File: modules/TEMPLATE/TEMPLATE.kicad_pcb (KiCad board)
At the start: 2 copper layers, 160 x 100 mm, 2 parts, among them J1 Card_Connector

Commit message: adsr additions
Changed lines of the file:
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@@
 		(rev "A")
 		(company "THE HOUSE OF GALAHAD")
-		(comment 1 "FORMANT-KO")
+		(comment 1 "FORMANT^{KO}")
 	)
 	(layers

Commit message: vc-lfo schematic; pcb start
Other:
- board text added: "${COMMENT1} ${TITLE}"
- board text added: "| ${COMMENT2} | ${COMMENT3} | ${COMMENT4} |"
- board text added: "| ${COMPANY} | ${COMMENT1} ${TITLE} | REV ${REVISION} | ${ISSUE_DATE} |"
- board text added: "| ${TITLE} | ${COMMENT5} |"
- board text removed: "| ${COMPANY} | ${COMMENT1} ${TITLE} | REVISION ${REVISION} | ${ISSUE_DATE} |"
- board text removed: "| ${EMAIL} | ${GITHUB} | ${TAG} |"
- board text removed: "| ${MODULE} | ${PARTNO} |"

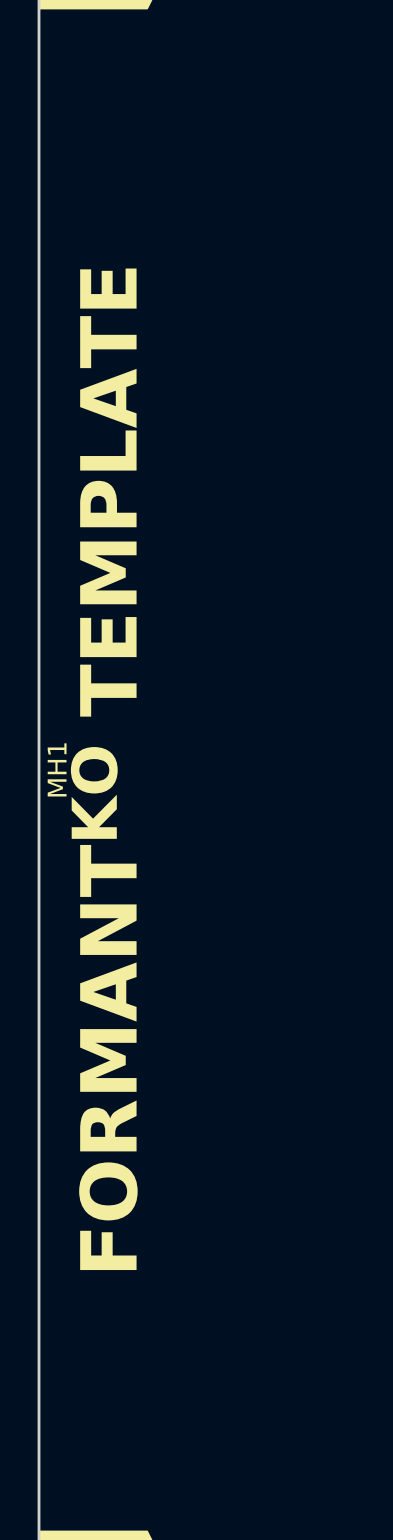
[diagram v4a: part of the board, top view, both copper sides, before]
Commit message: com updates for new templates and styles
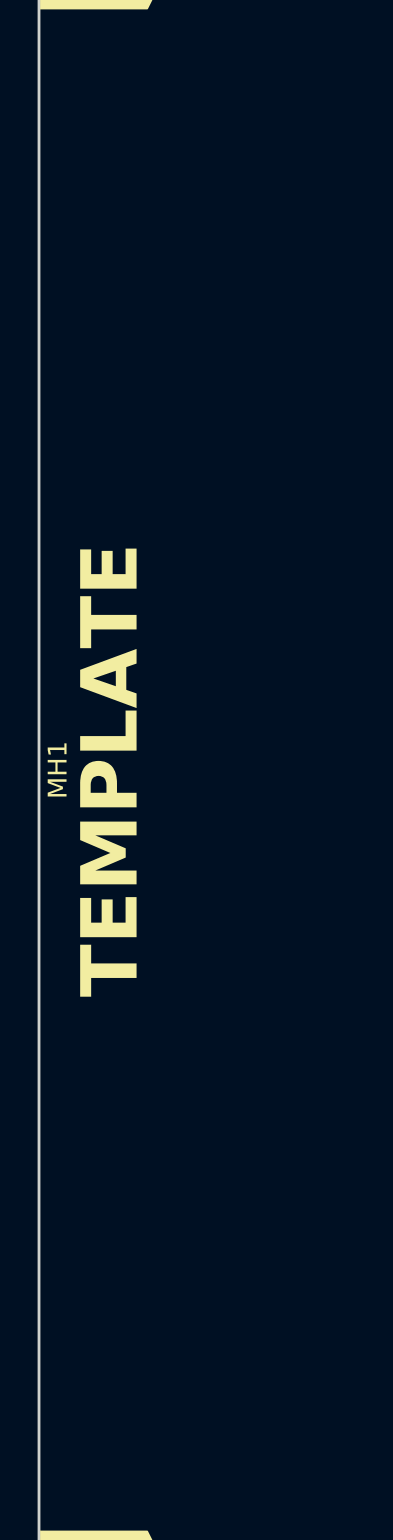
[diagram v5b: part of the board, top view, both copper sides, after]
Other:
- board text added: "${TITLE}"
- board text removed: "${COMMENT1} ${TITLE}"
